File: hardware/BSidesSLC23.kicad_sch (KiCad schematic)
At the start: 37 parts, among them J1 Conn_01x04, J2 Conn_02x03_Counter_Clockwise, J3 Conn_01x08, J4 EPD Connector, Q1 Si1308EDL, SW1 SW_Push, U1 STM8L051F3P, U2 W25Q80DVSN

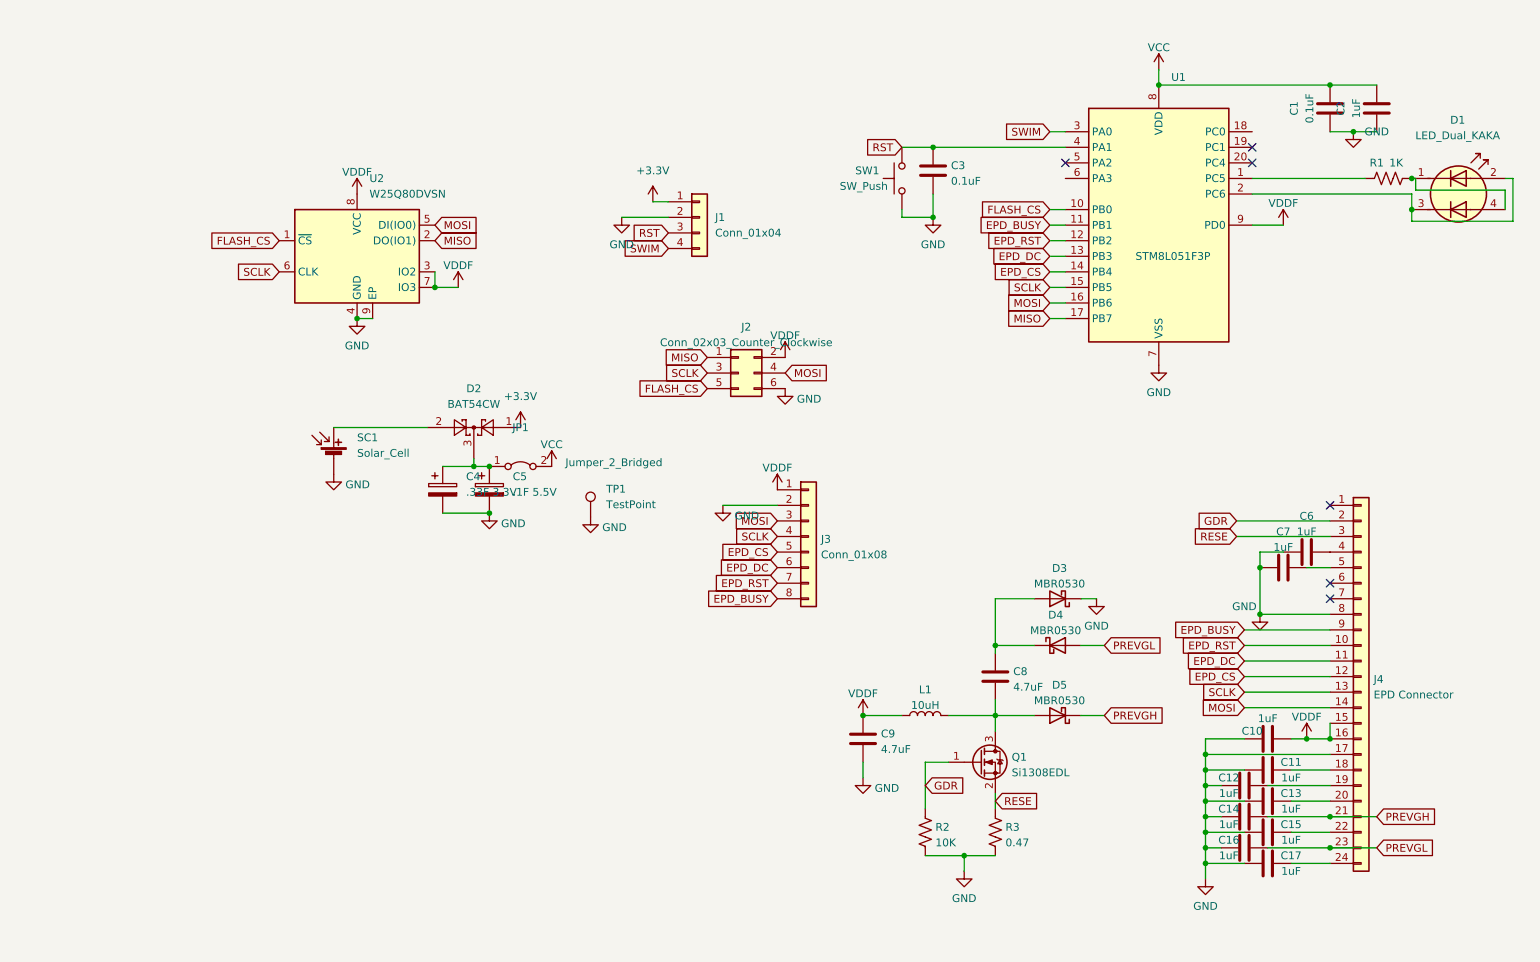
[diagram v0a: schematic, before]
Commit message: Added more images
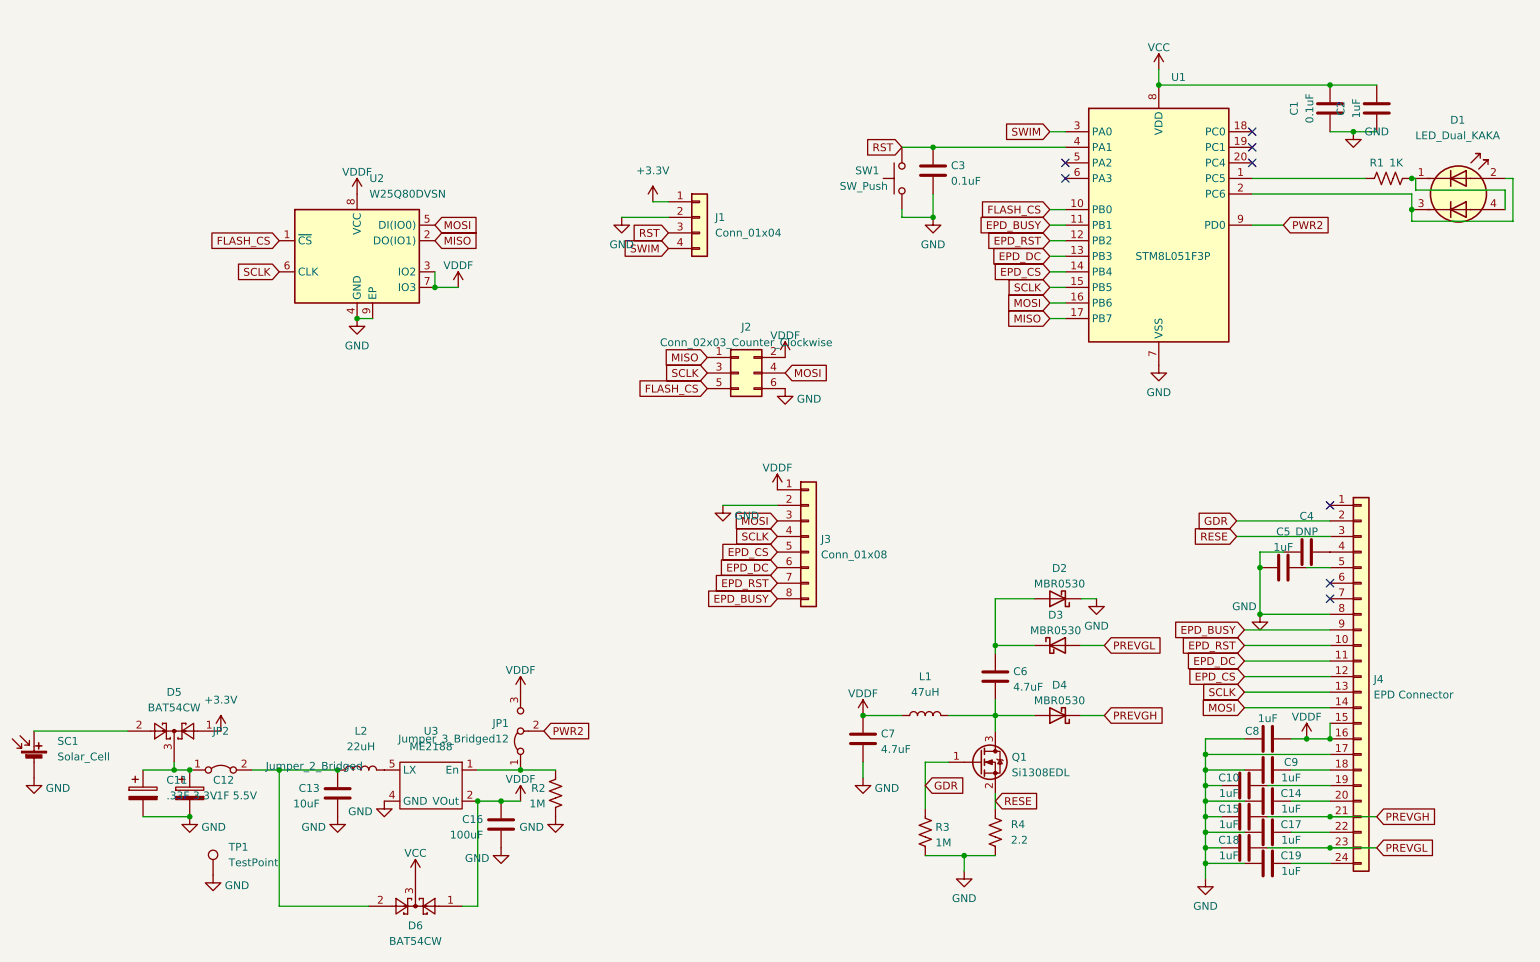
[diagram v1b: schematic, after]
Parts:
- added C13: 10uF, Capacitor_SMD:C_0603_1608Metric, symbol Device:C
- added C16: 100uF, Capacitor_SMD:C_0603_1608Metric, symbol Device:C
- added D6: BAT54CW, Package_TO_SOT_SMD:SOT-323_SC-70, symbol Diode:BAT54CW
- added JP1: Jumper_3_Bridged12, Jumper:SolderJumper-3_P1.3mm_Bridged12_RoundedPad1.0x1.5mm, symbol Jumper:Jumper_3_Bridged12
- added L2: 22uH, Inductor_SMD:L_Taiyo-Yuden_NR-30xx, symbol Device:L
- added R2: 1M, Resistor_SMD:R_0603_1608Metric, symbol Device:R_US
- added U3: ME2188, Package_TO_SOT_SMD:SOT-23-5, symbol Grange:ME2188
- C4: renamed from C6; value 1uF -> DNP
- L1: value 10uH -> 47uH
- R3: renamed from R2; value 10K -> 1M
- R4: renamed from R3; value 0.47 -> 2.2
- renumbered C12 to C10, C4 to C11, C5 to C12, C13 to C14, C14 to C15, C15 to C17, C16 to C18, C17 to C19, C7 to C5, C8 to C6, C9 to C7, C10 to C8, C11 to C9, D3 to D2, D4 to D3, D5 to D4, D2 to D5, JP1 to JP2
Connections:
- net GND: now also C13.2, C16.2, R2.2, U3.4 (GND)
- net VCC: now also D6.3; no longer JP2.2 (B)
- net VDDF: now also C16.1, D6.1, JP1.3 (B), U3.2 (VOut); no longer U1.9 (PD0)
- new net: JP1.1 (A), R2.1, U3.1 (En)
- new net: C13.1, D6.2, JP2.2 (B), L2.2
- new net: L2.1, U3.5 (LX)
- new net PWR2: JP1.2 (C), U1.9 (PD0)
- no-connect marks 6 -> 8
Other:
- moved on the sheet: C11, C12, D5, JP2, SC1, TP1

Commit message: Fixed LDO based on prototype
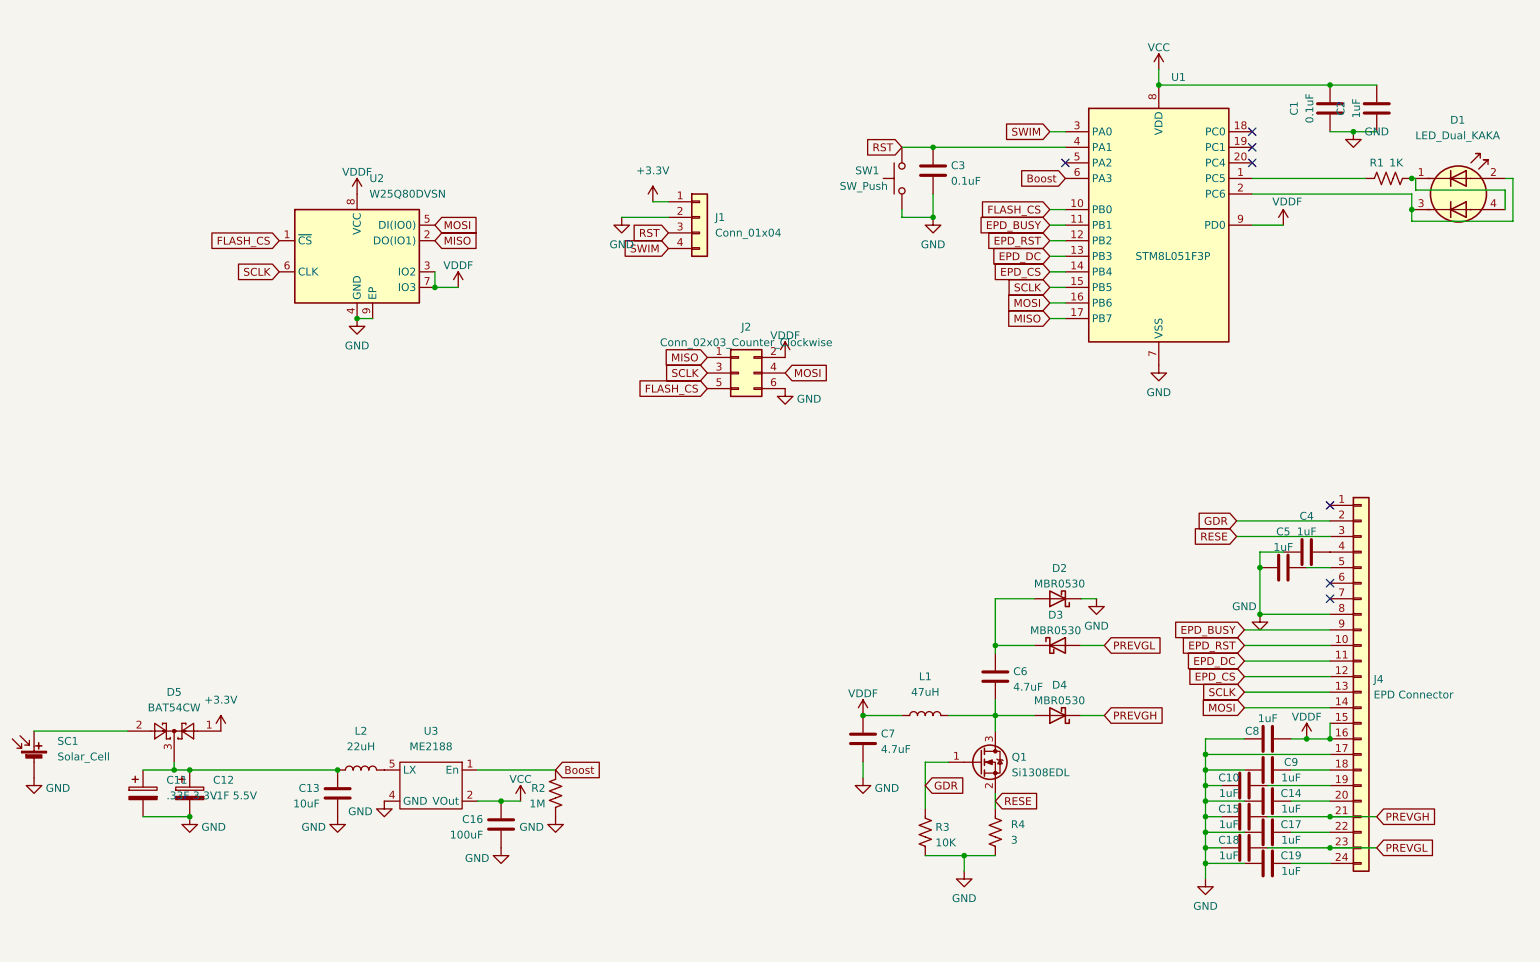
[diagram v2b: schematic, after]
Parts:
- removed D6: BAT54CW, Package_TO_SOT_SMD:SOT-323_SC-70, symbol Diode:BAT54CW
- removed J3: Conn_01x08, Connector_PinSocket_1.27mm:PinSocket_1x08_P1.27mm_Vertical, symbol Connector_Generic:Conn_01x08
- removed JP1: Jumper_3_Bridged12, Jumper:SolderJumper-3_P1.3mm_Bridged12_RoundedPad1.0x1.5mm, symbol Jumper:Jumper_3_Bridged12
- removed JP2: Jumper_2_Bridged, Jumper:SolderJumper-2_P1.3mm_Bridged_RoundedPad1.0x1.5mm, symbol Jumper:Jumper_2_Bridged
- removed TP1: TestPoint, TestPoint:TestPoint_Pad_D1.0mm, symbol Connector:TestPoint
- C12: footprint Capacitor_THT:CP_Radial_D13.0mm_P5.00mm -> Capacitor_THT:CP_Radial_D10.0mm_P5.00mm
- C4: value DNP -> 1uF
- R3: value 1M -> 10K
- R4: value 2.2 -> 3
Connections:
- net PWR2 is gone; now on net VDDF: U1.9 (PD0)
- net VCC: now also C16.1, U3.2 (VOut)
- net VDDF: no longer C16.1, U3.2 (VOut)
- net at C11.1, C12.1, D5.3: now also C13.1, L2.2
- net Boost: now reaches R2.1, U3.1 (En)
- net Boost: now also U1.6 (PA3)
- no-connect marks 8 -> 7

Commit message: Finializing hardware
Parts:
- removed C11: .33F 3.3V, Grange:DYNACAP, symbol Device:C_Polarized
- added R2, R3: 1K, Resistor_SMD:R_0603_1608Metric, symbol Device:R_US
- C11: renamed from C12; value .1F 5.5V -> HESC5R5104Z-H; footprint Capacitor_THT:CP_Radial_D10.0mm_P5.00mm -> Grange:HESC5R5104Z
- C15: renamed from C16; footprint Capacitor_SMD:C_0603_1608Metric -> Capacitor_SMD:C_1206_3216Metric
- D1: value LED_Dual_KAKA -> AAA3528SURKCGKC09
- J3: renamed from J4; value EPD Connector -> AFC34-S24FIA-00
- L1: value 47uH -> 10uH
- SC1: value Solar_Cell -> SM400K10L
- U3: value ME2188 -> ME2188C30M5G
- renumbered C13 to C12, C14 to C13, C15 to C14, C17 to C16, C18 to C17, C19 to C18, R2 to R4, R3 to R5, R4 to R6
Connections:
- net GND: now also R2.2, R3.2
- net Lock: now reaches U1.5 (PA2)
- net Lock: now also R2.1, R3.1
- no-connect marks 7 -> 6
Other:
- moved on the sheet: C1, C2

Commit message: Version 0.1 of hardware sent to fab shop
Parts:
- L2: footprint Inductor_SMD:L_Taiyo-Yuden_NR-30xx -> Inductor_SMD:L_Coilcraft_XxL4030
- U2: symbol Memory_Flash:W25Q32JVZP -> Memory_Flash:W25Q128JVS
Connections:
- net GND: no longer U2.9 (EP)
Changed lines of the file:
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@@
       (effects (font (size 1.27 1.27)) hide)
     )
-    (property "Datasheet" "~" (id 3) (at 252.73 120.65 0)
+    (property "Datasheet" "GDEY027T91" (id 3) (at 252.73 120.65 0)
       (effects (font (size 1.27 1.27)) hide)
     )
@@
     (pin "1")
   )
-  (symbol (lib_id "Memory_Flash:W25Q32JVZP") (at 88.9 52.07 0) (unit 1)
+  (symbol (lib_id "Memory_Flash:W25Q128JVS") (at 88.9 52.07 0) (unit 1)
     (in_bom yes) (on_board yes) (fields_autoplaced)
     (property "Reference" "U2" (id 0) (at 90.9194 39.37 0)
@@
       (effects (font (size 1.27 1.27)) hide)
     )
-    (property "Datasheet" "https://www.mouser.com/datasheet/2/949/w25q80dv_dl_revh_10022015-1489677.pdf" (id 3) (at 88.9 52.07 0)
+    (property "Datasheet" "http://www.winbond.com/resource-files/w25q80DVSN.pdf" (id 3) (at 88.9 52.07 0)
       (effects (font (size 1.27 1.27)) hide)
     )
@@
     (pin "7")
     (pin "8")
-    (pin "9")
   )
   (symbol (lib_id "power:GND") (at 115.57 90.805 0) (unit 1)
@@
     (property "Reference" "L2" (id 0) (at 89.535 129.54 90))
     (property "Value" "22uH" (id 1) (at 89.535 132.08 90))
-    (property "Footprint" "Inductor_SMD:L_Taiyo-Yuden_NR-30xx" (id 2) (at 89.535 135.89 0)
-      (effects (font (size 1.27 1.27)) hide)
-    )
-    (property "Datasheet" "~" (id 3) (at 89.535 135.89 0)
+    (property "Footprint" "Inductor_SMD:L_Coilcraft_XxL4030" (id 2) (at 89.535 135.89 0)
+      (effects (font (size 1.27 1.27)) hide)
+    )
+    (property "Datasheet" "XRCD43-220M" (id 3) (at 89.535 135.89 0)
       (effects (font (size 1.27 1.27)) hide)
     )
@@
     )
     (path "/832e7495-60ce-4d00-97ba-6acbcb51ceab"
-      (reference "L2") (unit 1) (value "22uH") (footprint "Inductor_SMD:L_Taiyo-Yuden_NR-30xx")
+      (reference "L2") (unit 1) (value "22uH") (footprint "Inductor_SMD:L_Coilcraft_XxL4030")
     )
     (path "/e10d4728-85cb-45ca-8558-44a7df209c08"
